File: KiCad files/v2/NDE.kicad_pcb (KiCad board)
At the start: 2 copper layers, 90 x 90 mm, 21 parts, among them J1 Nabíjací modul, J10 Conn_01x01_Socket, J11 Conn_01x01_Socket, J12 Conn_01x01_Socket, J13 Conn_01x01_Socket, J2 Step-up input, J3 Step-up output, J6 Conn_01x05_Socket, J7 Conn_01x08_Socket, J8 Conn_01x20_Socket, J9 Conn_01x20_Socket, U1 LM7805_TO220

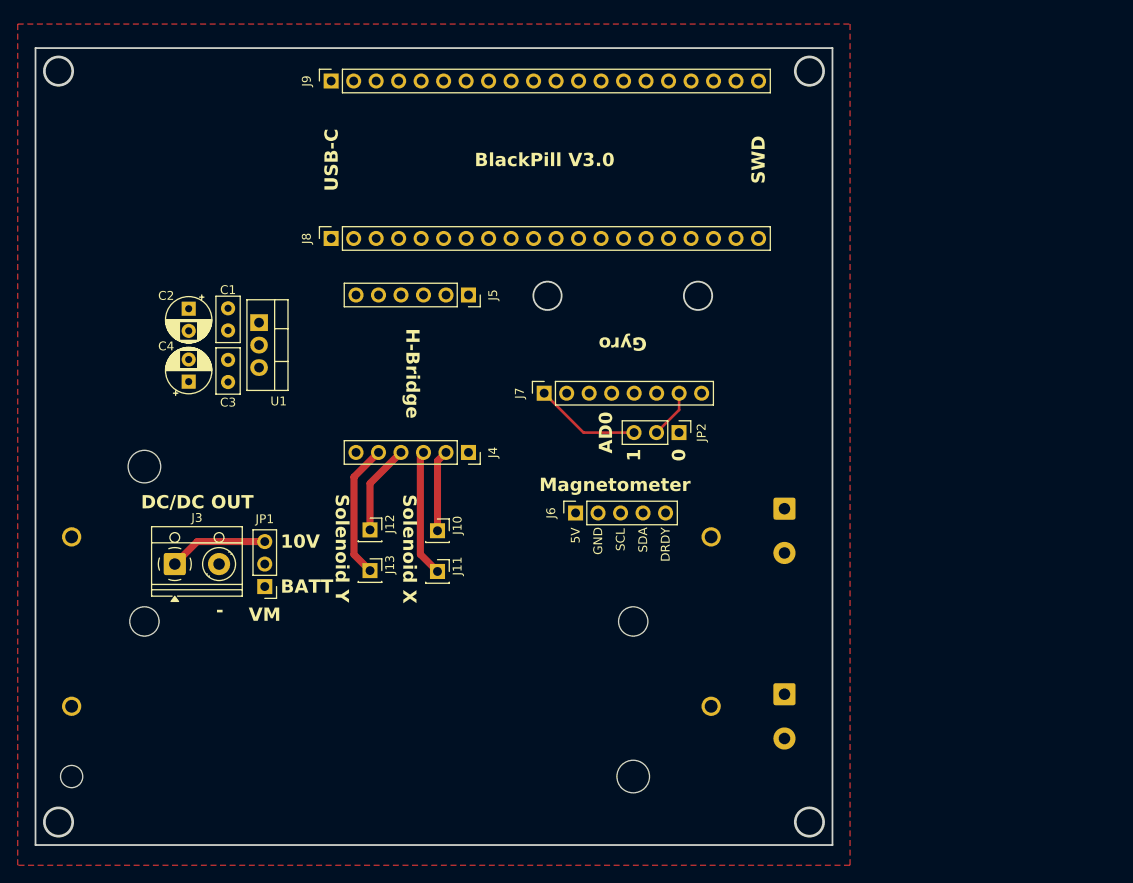
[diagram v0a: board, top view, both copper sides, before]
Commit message: Improved routing and layout
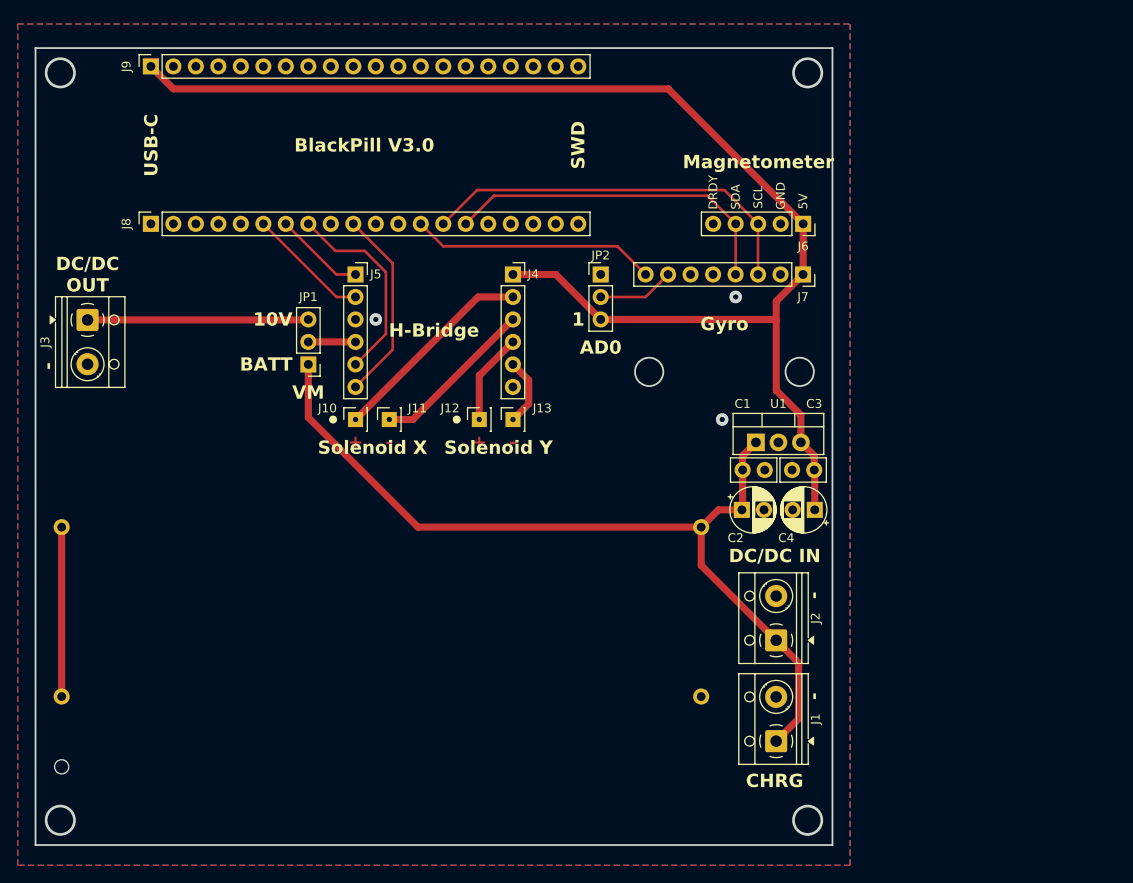
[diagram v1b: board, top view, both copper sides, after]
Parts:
- J1, J2: moved to F.Cu
- moved C4 72.2 mm to (188.0, 102.1), turned to 180 degrees
- moved C3 66.9 mm to (187.9, 97.6), turned to 180 degrees
- moved C2 66.5 mm to (179.8, 102.1), turned to 0 degrees
- moved C1 60.9 mm to (179.9, 97.6), turned to 0 degrees
- moved U1 57.7 mm to (181.4, 94.5), turned to 0 degrees
- moved J6 41.6 mm to (186.7, 69.8), turned to -90 degrees
- moved J7 32.2 mm to (186.7, 75.6), turned to -90 degrees
- moved J3 29.3 mm to (105.9, 80.7), turned to -90 degrees
- moved J1 26.3 mm to (183.6, 128.3), turned to 90 degrees
- moved JP1 25.6 mm to (130.8, 85.7)
- moved J13 23.5 mm to (153.9, 91.9), turned to 90 degrees
- moved J4 20.7 mm to (153.9, 75.6), turned to 0 degrees
- moved J8 20.4 mm to (113.0, 69.8)
- moved J9 20.4 mm to (113.0, 52.1)
- moved JP2 19.9 mm to (163.8, 75.6), turned to 0 degrees
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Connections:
- J5 pad 1: /BlackPill V3.0/A15 -> /BlackPill V3.0/A10
- J5 pad 2: /BlackPill V3.0/A11 -> /BlackPill V3.0/A9
- J5 pad 5: /BlackPill V3.0/A10 -> /BlackPill V3.0/A11
- J5 pad 6: /BlackPill V3.0/A9 -> /BlackPill V3.0/A15
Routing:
- net +5V: track 12.0 -> 148.3 mm
- net +BATT: track 0.00 -> 98.9 mm
- net /SCL1: track 0.00 -> 44.4 mm
- net /SDA1: track 0.00 -> 38.8 mm
- net /GY_INT: track 0.00 -> 27.8 mm
- net /BlackPill V3.0/A11: track 0.00 -> 22.9 mm
- net /BlackPill V3.0/A15: track 0.00 -> 22.0 mm
- net Net-(BT1-PadN1): track 0.00 -> 19.1 mm
- net /H-mostík/OUT1: track 9.64 -> 23.5 mm
- net /BlackPill V3.0/A9: track 0.00 -> 13.8 mm
- net +10V: track 11.2 -> 25.0 mm
- net /BlackPill V3.0/A10: track 0.00 -> 10.2 mm
- net /H-mostík/OUT4: track 15.3 -> 7.70 mm
- net /H-mostík/VCC: track 0.00 -> 5.32 mm
- net /H-mostík/OUT2: track 14.4 -> 18.6 mm
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- added copper zone on B.Cu, net GND
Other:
- outline, holes or cut-outs redrawn
- board text added: "+"
- board text added: "X"
- board text added: "Y"
- board text removed: "0"

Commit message: v2 ready for manufacturing
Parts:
- added H1: MountingHole, MountingHole:MountingHole_3.2mm_M3_ISO14580, F.Cu at (102.8, 52.8)
- added H2: MountingHole, MountingHole:MountingHole_3.2mm_M3_ISO14580, F.Cu at (187.2, 52.8)
- added H3: MountingHole, MountingHole:MountingHole_3.2mm_M3_ISO14580, F.Cu at (102.8, 137.2)
- added H4: MountingHole, MountingHole:MountingHole_3.2mm_M3_ISO14580, F.Cu at (187.2, 137.2)
- added H5: MountingHole, MountingHole:MountingHole_3.2mm_M3_ISO14580, F.Cu at (170.3, 85.6)
- added H6: MountingHole, MountingHole:MountingHole_3.2mm_M3_ISO14580, F.Cu at (185.3, 85.6)
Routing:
- net +BATT: track 98.9 -> 99.5 mm
- net GND: vias 3 -> 4
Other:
- outline, holes or cut-outs redrawn
- board text added: "Christopher Kois/Magnetorquer/BOTTOM"
- board text added: "Christopher Kois/Magnetorquer/TOP"
- board text added: "Magnetorquer Module Control Board"

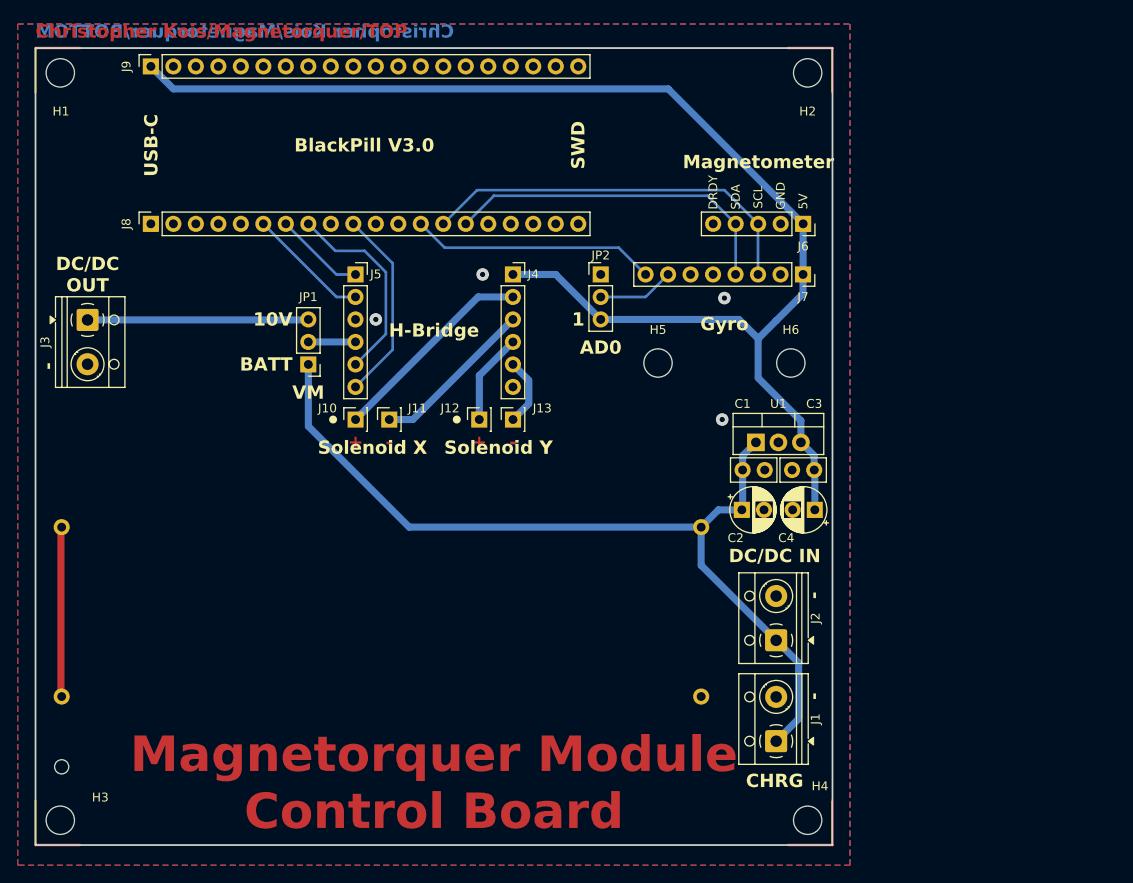
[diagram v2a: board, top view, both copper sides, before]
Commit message: Modified text for top layer
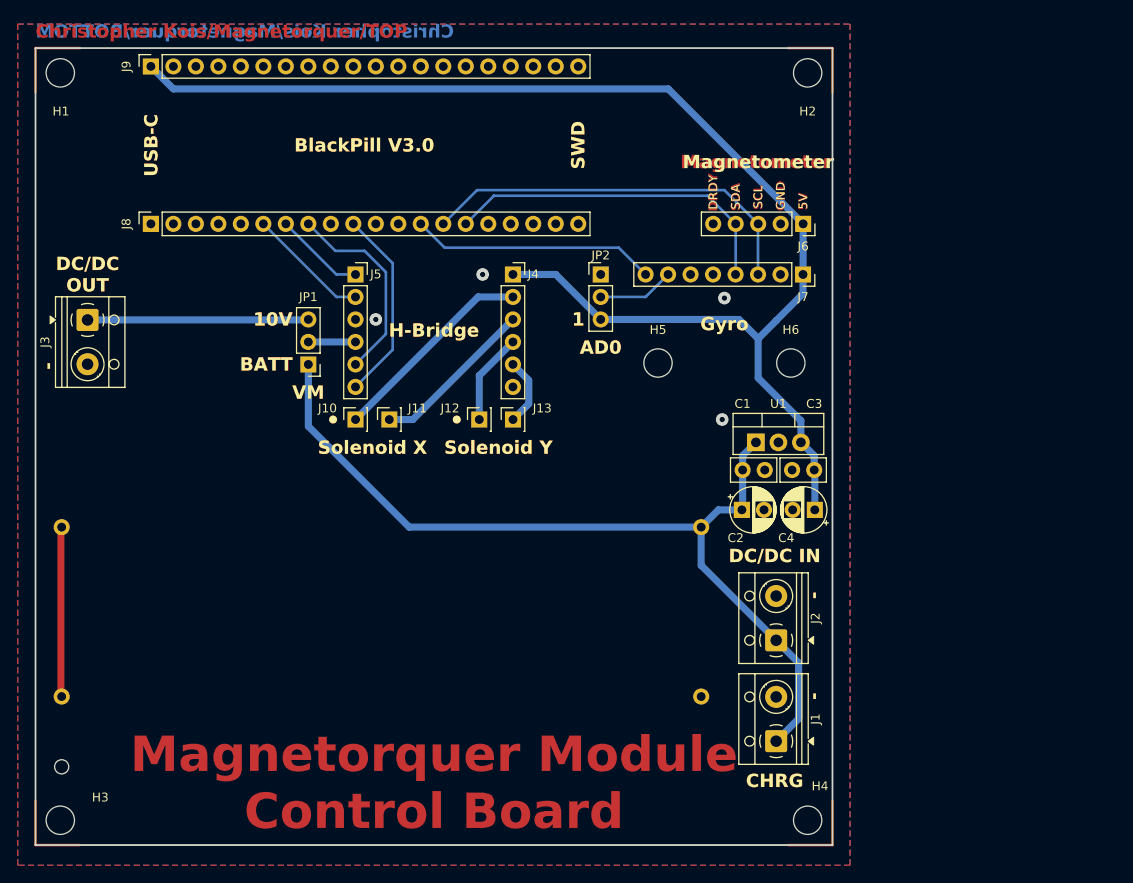
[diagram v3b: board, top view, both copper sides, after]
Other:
- board text removed: "+"
- board text removed: "X"
- board text removed: "Y"

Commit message: Added models
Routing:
- net /BlackPill V3.0/A15: track 22.0 -> 22.8 mm
- net /SCL1: track 44.4 -> 45.1 mm
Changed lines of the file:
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@@
 		)
 		(embedded_fonts no)
-		(model "${KICAD9_3DMODEL_DIR}/TerminalBlock_RND.3dshapes/TerminalBlock_RND_205-00012_1x02_P5.00mm_Horizontal.wrl"
+		(model "${KIPRJMOD}/Modely/RND 205-00012--3DModel-STEP-56544.STEP"
 			(offset
 				(xyz 0 0 0)
@@
 			)
 			(rotate
-				(xyz 0 0 0)
+				(xyz -90 -0 -180)
 			)
 		)
@@
 		)
 		(embedded_fonts no)
-		(model "${KICAD9_3DMODEL_DIR}/TerminalBlock_RND.3dshapes/TerminalBlock_RND_205-00012_1x02_P5.00mm_Horizontal.wrl"
+		(model "${KIPRJMOD}/Modely/RND 205-00012--3DModel-STEP-56544.STEP"
 			(offset
 				(xyz 0 0 0)
@@
 			)
 			(rotate
-				(xyz 0 0 0)
+				(xyz -90 -0 -180)
 			)
 		)
@@
 		)
 		(embedded_fonts no)
-		(model "${KICAD9_3DMODEL_DIR}/TerminalBlock_RND.3dshapes/TerminalBlock_RND_205-00012_1x02_P5.00mm_Horizontal.wrl"
+		(model "${KIPRJMOD}/Modely/RND 205-00012--3DModel-STEP-56544.STEP"
 			(offset
 				(xyz 0 0 0)
@@
 			)
 			(rotate
-				(xyz 0 0 0)
+				(xyz -90 -0 -180)
 			)
 		)
@@
 		)
 		(embedded_fonts no)
+		(model "${KIPRJMOD}/Modely/1049/1049-edit.STEP"
+			(offset
+				(xyz 0 9.5 0)
+			)
+			(scale
+				(xyz 1 1 1)
+			)
+			(rotate
+				(xyz -90 -0 90)
+			)
+		)
 	)
 	(gr_line
@@
 	)
 	(segment
-		(start 130.81 69.85)
-		(end 133.858 72.898)
+		(start 133.858 72.898)
+		(end 137.16 72.898)
 		(width 0.3)
 		(layer "B.Cu")
@@
 	)
 	(segment
-		(start 139.573 75.311)
-		(end 139.573 82.287)
+		(start 130.81 69.85)
+		(end 133.858 72.898)
 		(width 0.3)
 		(layer "B.Cu")
@@
 	)
 	(segment
-		(start 137.16 72.898)
-		(end 139.573 75.311)
+		(start 140 81.86)
+		(end 136.135 85.725)
 		(width 0.3)
 		(layer "B.Cu")
@@
 	)
 	(segment
-		(start 139.573 82.287)
-		(end 136.135 85.725)
+		(start 140 75.738)
+		(end 140 81.86)
 		(width 0.3)
 		(layer "B.Cu")
@@
 	)
 	(segment
-		(start 133.858 72.898)
-		(end 137.16 72.898)
+		(start 137.16 72.898)
+		(end 140 75.738)
 		(width 0.3)
 		(layer "B.Cu")
@@
 	)
 	(segment
-		(start 140.335 84.065)
-		(end 140.335 74.295)
+		(start 141.25 83.15)
+		(end 141.25 75.21)
 		(width 0.3)
 		(layer "B.Cu")
@@
 	)
 	(segment
-		(start 136.135 88.265)
-		(end 140.335 84.065)
+		(start 141.25 75.21)
+		(end 135.89 69.85)
 		(width 0.3)
 		(layer "B.Cu")
@@
 	)
 	(segment
-		(start 140.335 74.295)
-		(end 135.89 69.85)
+		(start 136.135 88.265)
+		(end 141.25 83.15)
 		(width 0.3)
 		(layer "B.Cu")
@@
 	)
 	(segment
-		(start 181.61 69.85)
-		(end 177.8 66.04)
+		(start 181.595 75.565)
+		(end 181.595 69.865)
 		(width 0.3)
 		(layer "B.Cu")
@@
 	)
 	(segment
-		(start 181.595 75.565)
-		(end 181.595 69.865)
+		(start 181.595 69.865)
+		(end 181.61 69.85)
 		(width 0.3)
 		(layer "B.Cu")
@@
 	)
 	(segment
-		(start 177.8 66.04)
-		(end 149.86 66.04)
+		(start 177.01 65.25)
+		(end 150.65 65.25)
 		(width 0.3)
 		(layer "B.Cu")
@@
 	)
 	(segment
-		(start 181.595 69.865)
-		(end 181.61 69.85)
+		(start 150.65 65.25)
+		(end 146.05 69.85)
 		(width 0.3)
 		(layer "B.Cu")
@@
 	)
 	(segment
-		(start 149.86 66.04)
-		(end 146.05 69.85)
+		(start 181.61 69.85)
+		(end 177.01 65.25)
 		(width 0.3)
 		(layer "B.Cu")

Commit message: Update
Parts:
- added J4: ~, Connector_PinSocket_2.54mm:PinSocket_1x06_P2.54mm_Vertical, F.Cu at (203.2, 50.8)
- added J4: ~, Connector_PinSocket_2.54mm:PinSocket_1x06_P2.54mm_Vertical, F.Cu at (218.4, 50.8)
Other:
- board text added: "PCB3D_BR_NDE"
- board text added: "PCB3D_TL_NDE"
